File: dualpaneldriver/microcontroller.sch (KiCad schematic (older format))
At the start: 54 parts, among them J401 PIR1, J402 Conn_01x02, J403 PIR2, J404 HALL, J405 PIR3, J406 WS2812CTRL, J407 I2C, J408 CAN, J409 Conn_ARM_JTAG_SWD_10, J410 UART, J411 CAN, Q401 AO3400, SW401 POWERON, U401 STM32F072C8Tx, U402 OPT3001, U403 SN65HVD232, Y401 8.000MHz

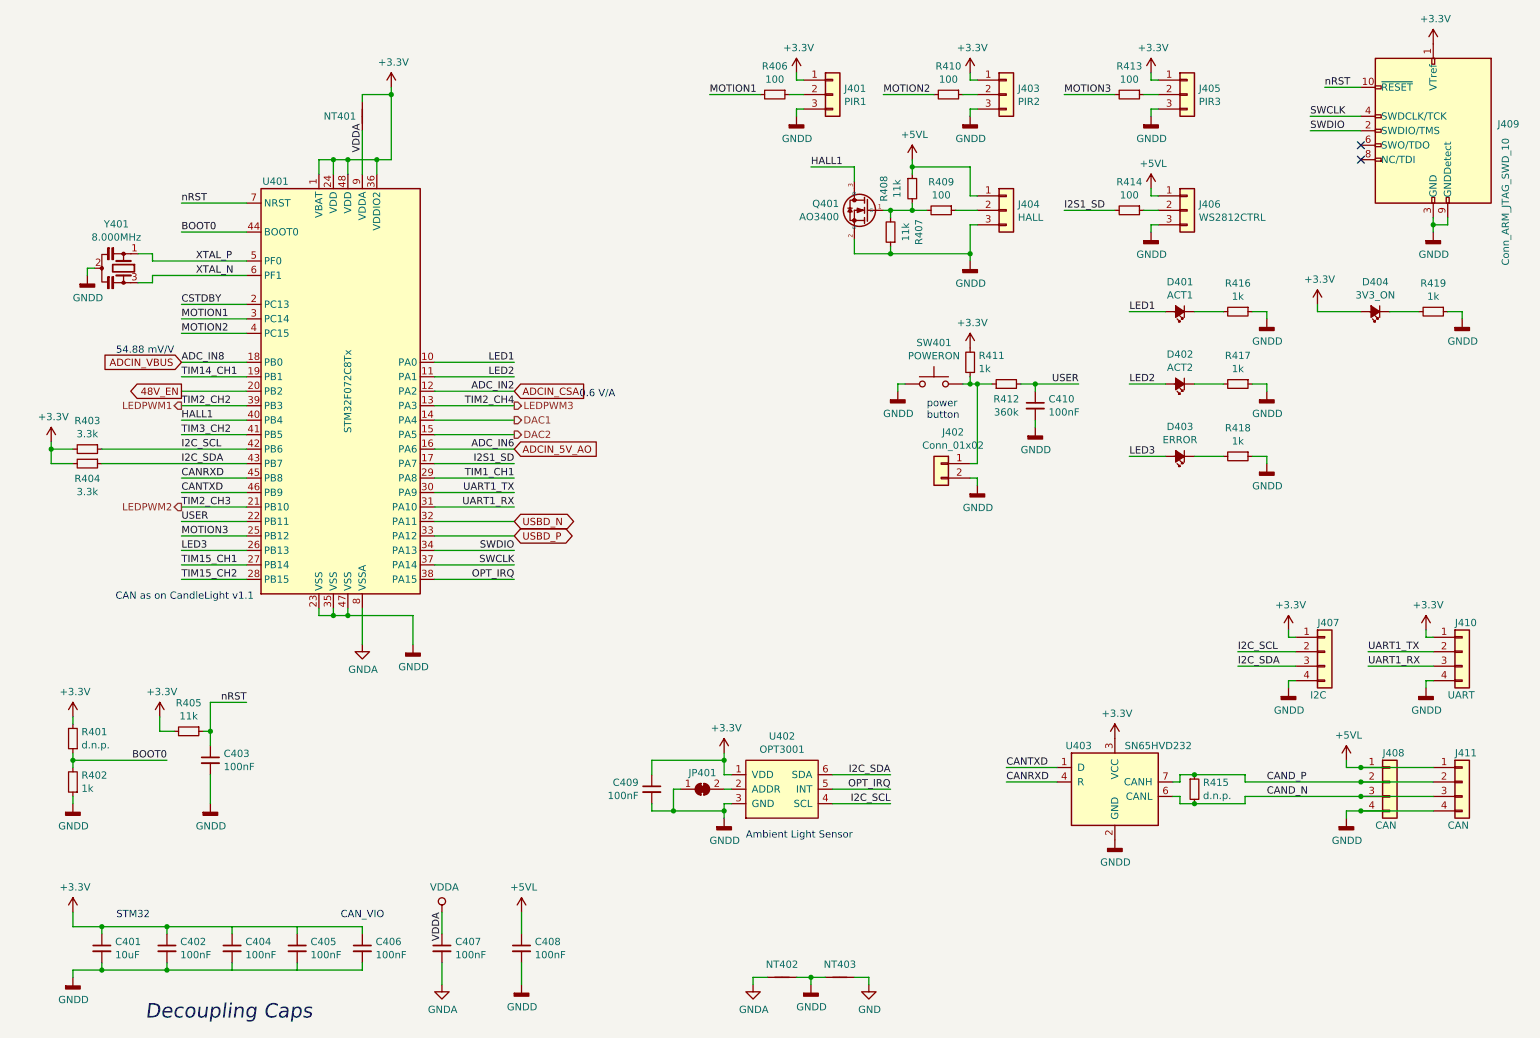
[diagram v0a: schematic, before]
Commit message: added Hall Op Amp
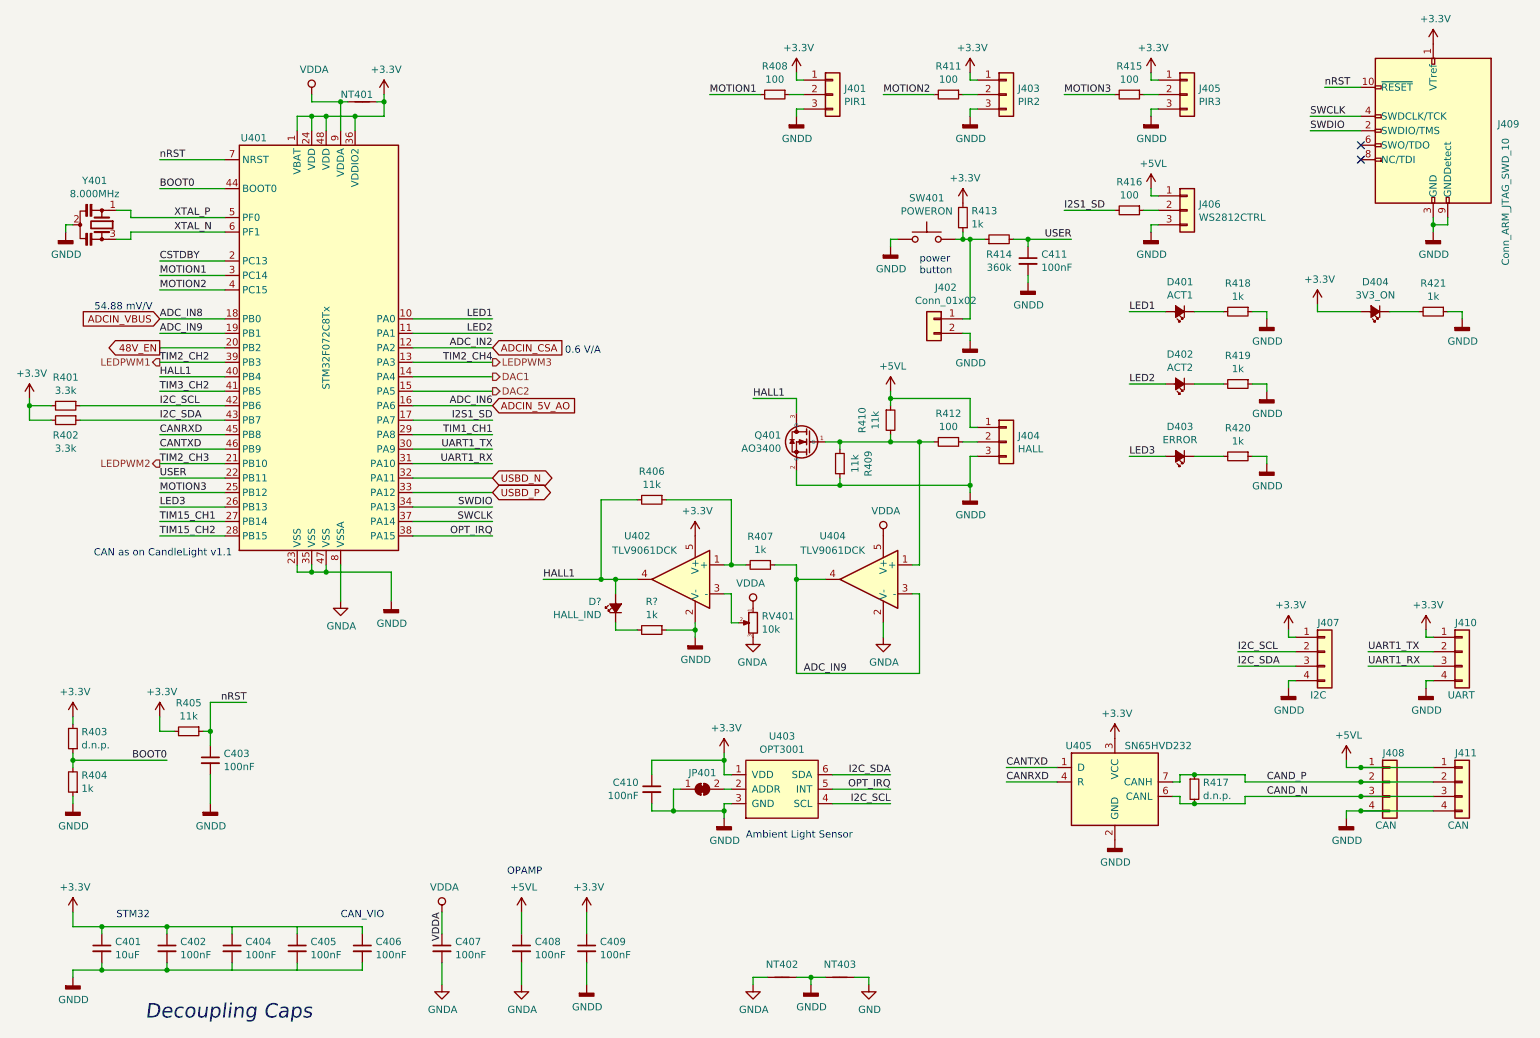
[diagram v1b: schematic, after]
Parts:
- added C409: 100nF, Capacitor_SMD:C_0603_1608Metric, symbol Device:C_Small
- added D?: HALL_IND, LED_SMD:LED_0603_1608Metric, symbol Device:LED_Small_ALT
- added R406: 11k, Resistor_SMD:R_0603_1608Metric, symbol Device:R_Small
- added R407, R?: 1k, Resistor_SMD:R_0603_1608Metric, symbol Device:R_Small
- added RV401: 10k, symbol Device:R_POT_Small
- added U402, U404: TLV9061DCK, Automated:Texas_R-PDSO-G5, symbol meansOfCircuitDesign:TLV9061DCK
- renumbered C409 to C410, C410 to C411, R403 to R401, R404 to R402, R401 to R403, R402 to R404, R406 to R408, R407 to R409, R408 to R410, R410 to R411, R409 to R412, R411 to R413, R412 to R414, R413 to R415, R414 to R416, R415 to R417, R416 to R418, R417 to R419, R418 to R420, R419 to R421, U402 to U403, U403 to U405
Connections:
- net +3V3: now also C409.1, U402.5 (V+)
- net GNDA: now also C408.2, RV401.3, U404.2 (V-)
- net GNDD: now also C409.2, R?.1, U402.2 (V-); no longer C408.2
- net HALL1: now also D?.2 (A), R406.2, U402.4
- net VDDA: now also RV401.1, U404.5 (V+)
- net at Q401.1 (G), R409.2, R410.2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: now also U404.1 (+)
- net TIM14_CH1 renamed ADC_IN9
- net ADC_IN9: now also R407.1, U404.3 (-), U404.4
- new net: RV401.2, U402.3 (-)
- new net: R406.1, R407.2, U402.1 (+)
- new net: D?.1 (K), R?.2
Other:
- note added: "OPAMP"
- moved on the sheet: C411, J402, J404, NT401, Q401, R401, R402, R409, R410, R412, R413, R414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

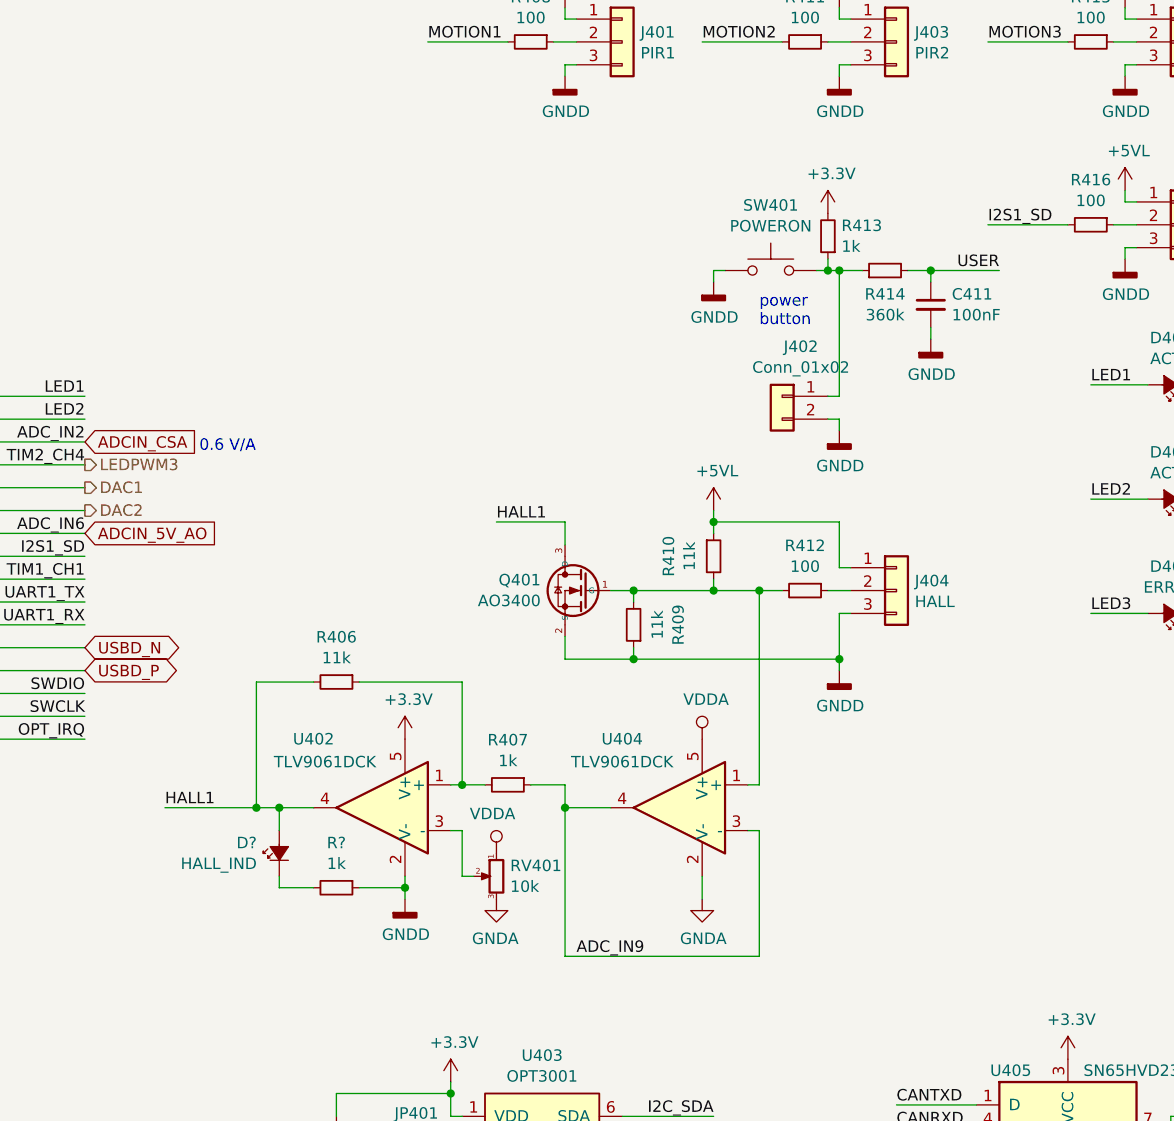
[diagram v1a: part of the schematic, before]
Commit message: removed op amp
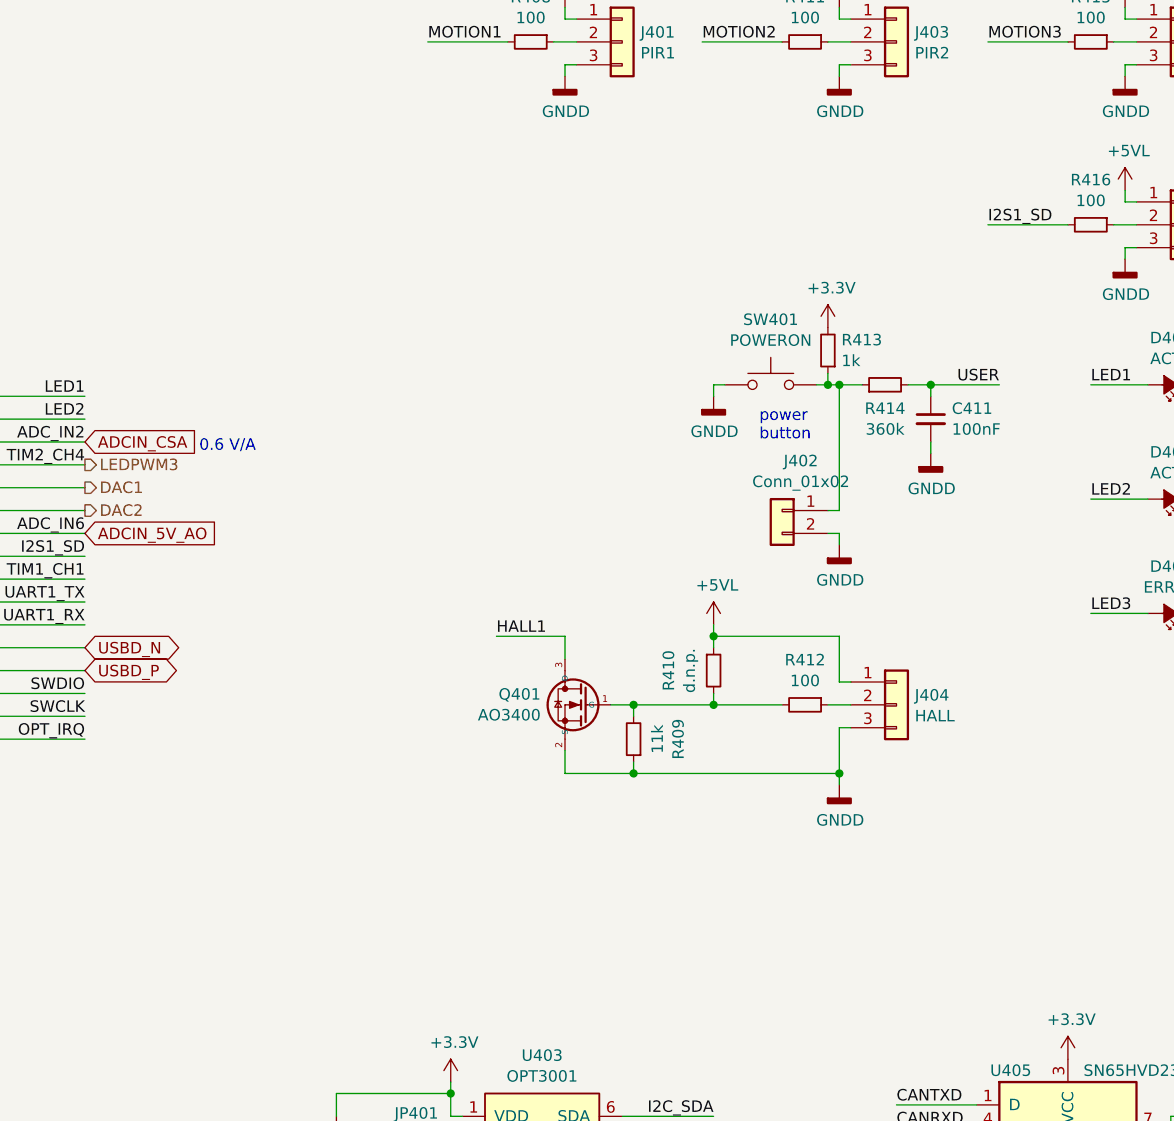
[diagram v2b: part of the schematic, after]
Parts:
- removed D?: HALL_IND, LED_SMD:LED_0603_1608Metric, symbol Device:LED_Small_ALT
- removed R406: 11k, Resistor_SMD:R_0603_1608Metric, symbol Device:R_Small
- removed R407, R?: 1k, Resistor_SMD:R_0603_1608Metric, symbol Device:R_Small
- removed RV401: 10k, symbol Device:R_POT_Small
- removed U402, U404: TLV9061DCK, Automated:Texas_R-PDSO-G5, symbol meansOfCircuitDesign:TLV9061DCK
- R410: value 11k -> d.n.p.
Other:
- moved on the sheet: C411, J402, J404, Q401, R409, R410, R412, R413, R414, SW401

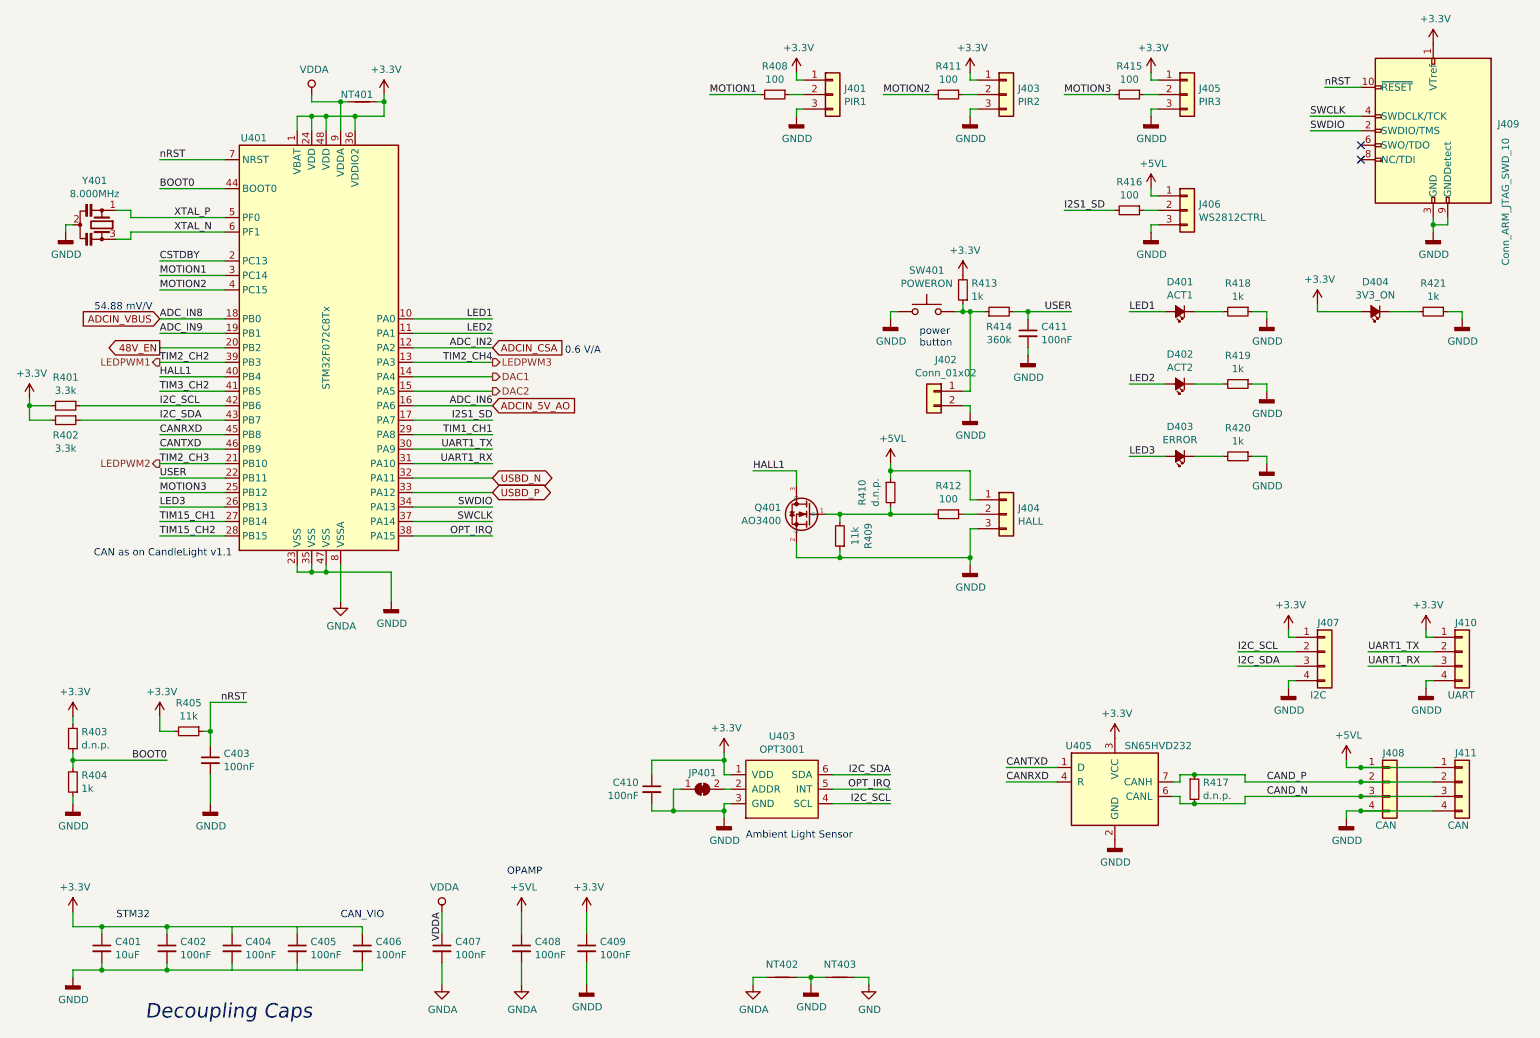
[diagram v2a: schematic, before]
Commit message: some components placed
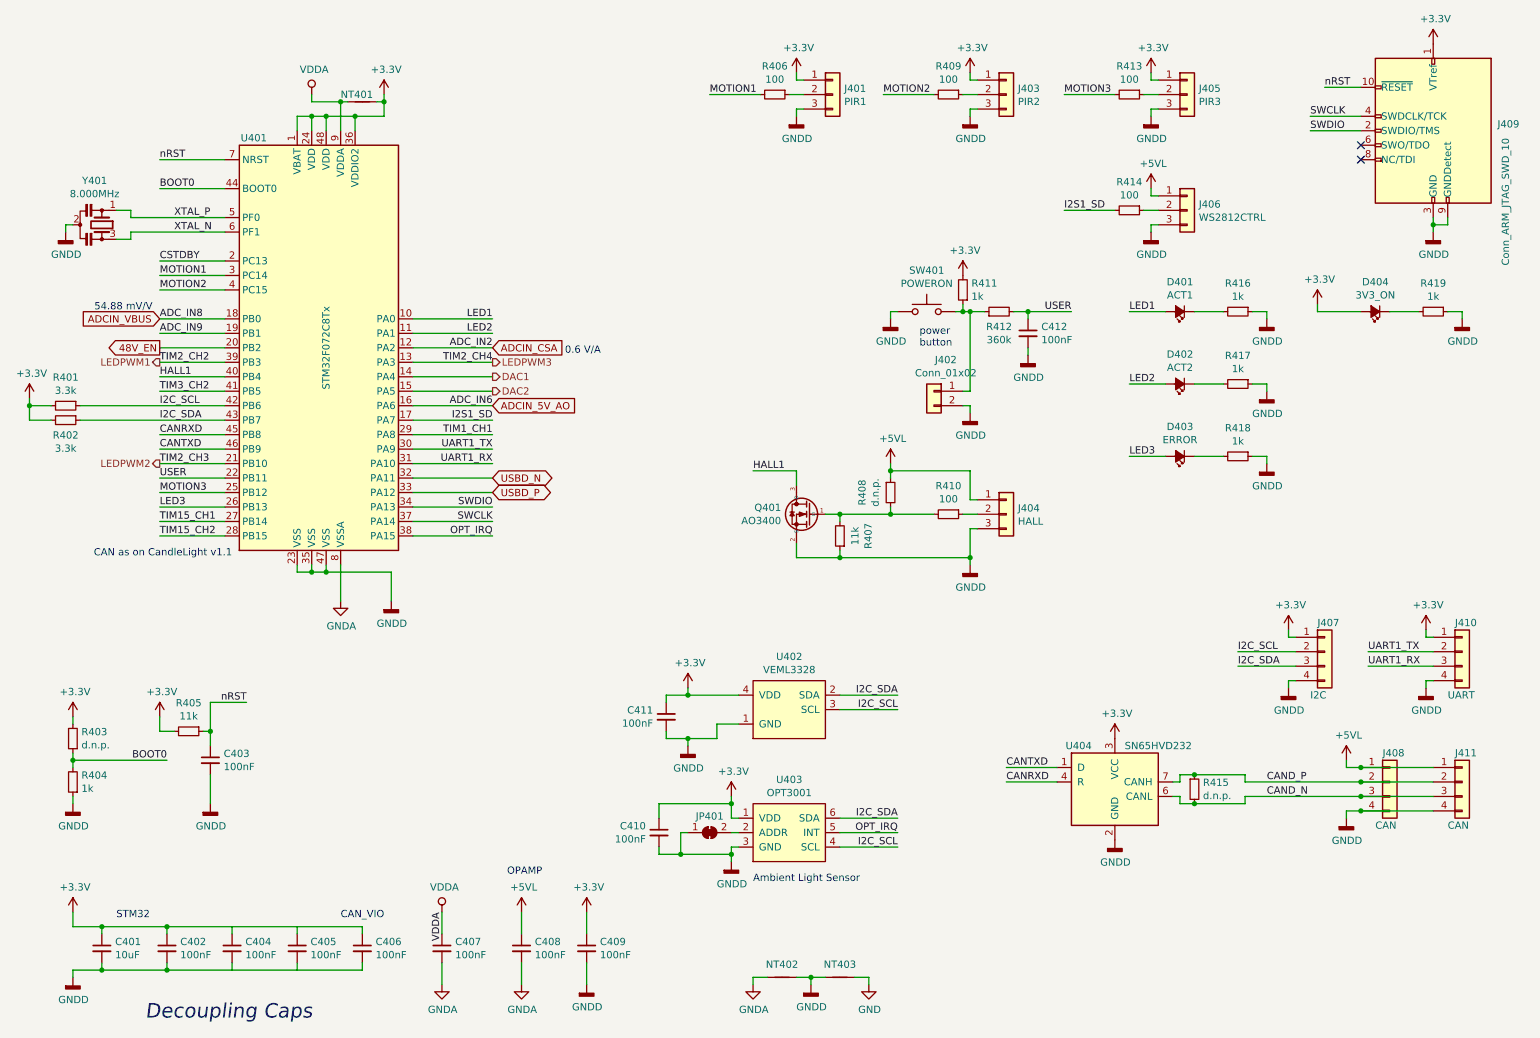
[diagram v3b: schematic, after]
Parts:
- added C411: 100nF, Capacitor_SMD:C_0603_1608Metric, symbol Device:C_Small
- added U402: VEML3328, Automated:Vishay_LGA-4_VEML_2x1.25mm, symbol meansOfCircuitDesign:VEML3328
- J401, J403, J404, J405, J406: footprint (none) -> Connector_PinHeader_2.54mm:PinHeader_1x03_P2.54mm_Vertical
- Q401: footprint (none) -> Package_TO_SOT_SMD:SOT-23
- renumbered C411 to C412, R408 to R406, R409 to R407, R410 to R408, R411 to R409, R412 to R410, R413 to R411, R414 to R412, R415 to R413, R416 to R414, R417 to R415, R418 to R416, R419 to R417, R420 to R418, R421 to R419, U405 to U404
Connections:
- net +3V3: now also C411.1, U402.4 (VDD)
- net GNDD: now also C411.2, U402.1 (GND)
- net I2C_SCL: now also U402.3 (SCL)
- net I2C_SDA: now also U402.2 (SDA)
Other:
- moved on the sheet: C410, JP401, U403
